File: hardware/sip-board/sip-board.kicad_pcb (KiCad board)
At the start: 8 copper layers, 17 x 50 mm, 110 parts, among them IC1 MT25QL512ABB1EW9-0SIT, IC2 XC7S15-1CPGA196C, IC3 LTC3569EUDC#TRPBF, J1 Conn_02x03_Odd_Even, J2 Conn_01x10_Pin, J3 Conn_01x10_Pin, J4 Conn_01x10_Pin, J5 Conn_01x10_Pin, Q1 MBT3904DW1, Q2 MBT3904DW1, Q5 BS170F

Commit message: WE REDOIN PCB
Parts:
- C10, C13, C15, C31, C32, C34, C36: footprint Capacitor_SMD:C_0201_0603Metric -> Capacitor_SMD:C_0402_1005Metric
- C11, C38: footprint Capacitor_SMD:C_0402_1005Metric -> Capacitor_SMD:C_0603_1608Metric; moved to B.Cu
- C2, C3, C39, C4, C5, C6, L1, L2, L3, R10, R11, R12, R13, R14, R15, R16, R17, R18, R19, R20, R25, R28, R30, R32, R4, R5, R6, R7, R8, R9, U10, U11, U12, U13, U4, U5, U6, U7, U8, U9: moved to F.Cu
- C28, C29, C30: footprint Capacitor_SMD:C_0402_1005Metric -> Capacitor_SMD:C_0603_1608Metric
- C33, C35: footprint Capacitor_SMD:C_0201_0603Metric -> Capacitor_SMD:C_0402_1005Metric; moved to F.Cu
- C37: footprint Capacitor_SMD:C_0201_0603Metric -> Capacitor_SMD:C_0603_1608Metric
- C8: footprint Capacitor_SMD:C_0201_0603Metric -> Capacitor_SMD:C_0603_1608Metric; moved to F.Cu
- moved R5 98.0 mm to (19.9, 57.5), turned to 0 degrees
- moved R7 97.2 mm to (19.9, 61.0), turned to 0 degrees
- moved R8 96.1 mm to (19.9, 62.8), turned to 0 degrees
- moved R9 95.2 mm to (19.9, 64.5), turned to 0 degrees
- moved C37 90.9 mm to (19.9, 54.0), turned to 0 degrees
- moved CFG1 90.6 mm to (25.1, 59.2), turned to 0 degrees
- moved U13 89.7 mm to (43.3, 40.2)
- moved U7 86.6 mm to (39.4, 36.5), turned to 0 degrees
- moved U12 85.8 mm to (43.3, 36.5)
- moved R20 85.3 mm to (40.9, 49.9), turned to 0 degrees
- moved J1 85.0 mm to (24.8, 67.7)
- moved U5 84.7 mm to (39.4, 29.2), turned to 0 degrees
- moved U11 81.6 mm to (43.3, 32.8)
- moved R19 81.5 mm to (40.9, 48.2), turned to 0 degrees
- moved R14 80.7 mm to (38.5, 48.2), turned to 0 degrees
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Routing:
- net +5V: track 141.0 -> 0.00 mm, vias 11 -> 0
- net GND: track 87.8 -> 0.00 mm, vias 97 -> 0
- net +3V3: track 61.4 -> 0.00 mm, vias 35 -> 0
- net SPI_DQ0: track 25.3 -> 0.00 mm, vias 2 -> 0
- net M0_CONFIG: track 24.9 -> 0.00 mm, vias 2 -> 0
- net M1_CONFIG: track 23.2 -> 0.00 mm, vias 4 -> 0
- net SPI_DQ3: track 23.2 -> 0.00 mm, vias 2 -> 0
- net SPI_DQ2: track 23.0 -> 0.00 mm, vias 2 -> 0
- net SPI_SCK_CCLK: track 22.7 -> 0.00 mm, vias 2 -> 0
- net SPI_DQ1: track 21.9 -> 0.00 mm, vias 2 -> 0
- net M2_CONFIG: track 21.8 -> 0.00 mm, vias 2 -> 0
- net +1V8: track 21.6 -> 0.00 mm, vias 6 -> 0
- net SPI_CS: track 21.2 -> 0.00 mm, vias 2 -> 0
- net +1V0: track 15.6 -> 0.00 mm, vias 12 -> 0
- net PROGRAM_B: track 15.1 -> 0.00 mm, vias 2 -> 0
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- removed copper zone on In3.Cu, net +1V0
- removed copper zone on In3.Cu, net +1V8
- removed copper zone on In4.Cu, net +3V3
- removed copper zone on In1.Cu, net GND
- removed copper zone on In6.Cu, net GND
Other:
- board text added: "3V3 1V8 1V0 GND"
- board text removed: "1V0"
- board text removed: "1V8"
- board text removed: "DQ0 SCK DQ3"
- board text removed: "DQ2 DQ1 __ CS"
- board text removed: "GND"
- board text removed: "INIT"
- board text removed: "JTAG"
- board text removed: "M2 M1 M0"
- board text removed: "M[2:0]=001 QSPI M[2:0]=101 JTAG"
- board text removed: "RESET"

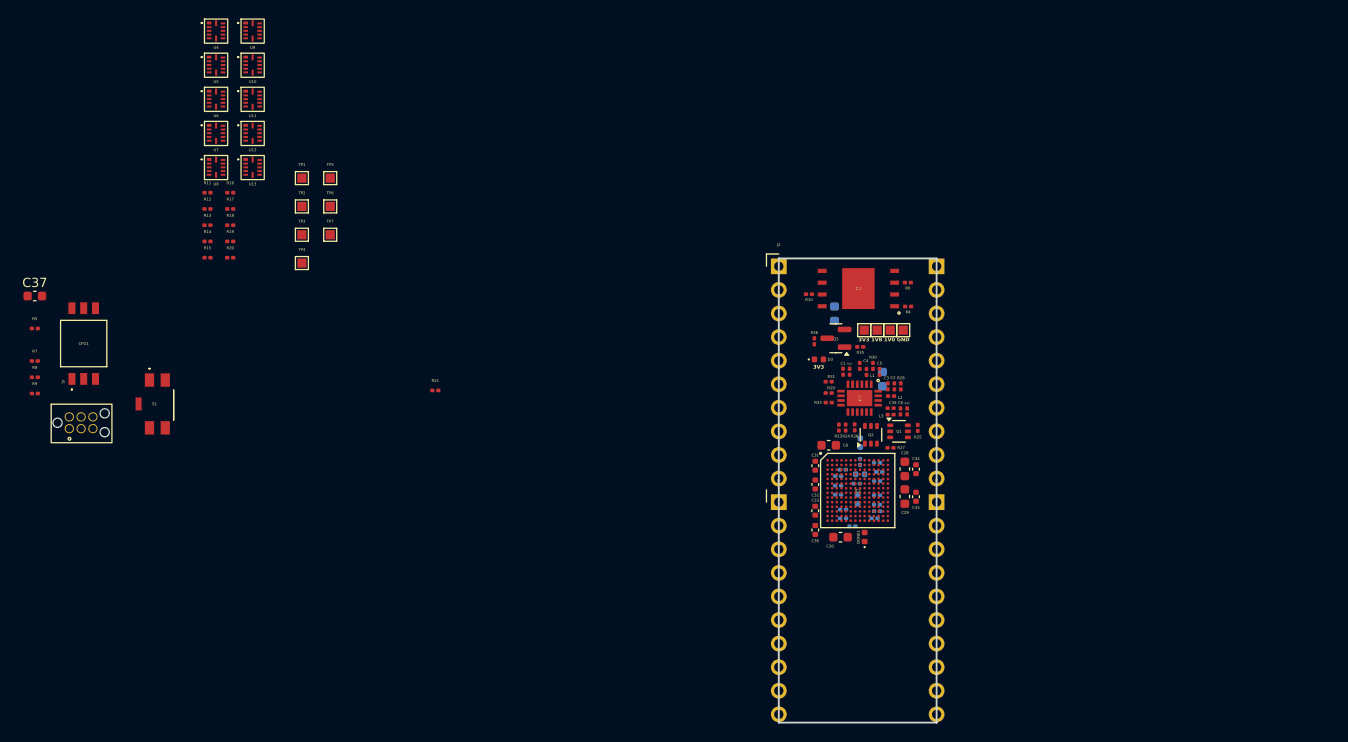
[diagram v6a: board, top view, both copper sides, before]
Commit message: redo layout of sip (again), changed switching reg to be on surface, need to route, need to add 2 more layers for 5V plane
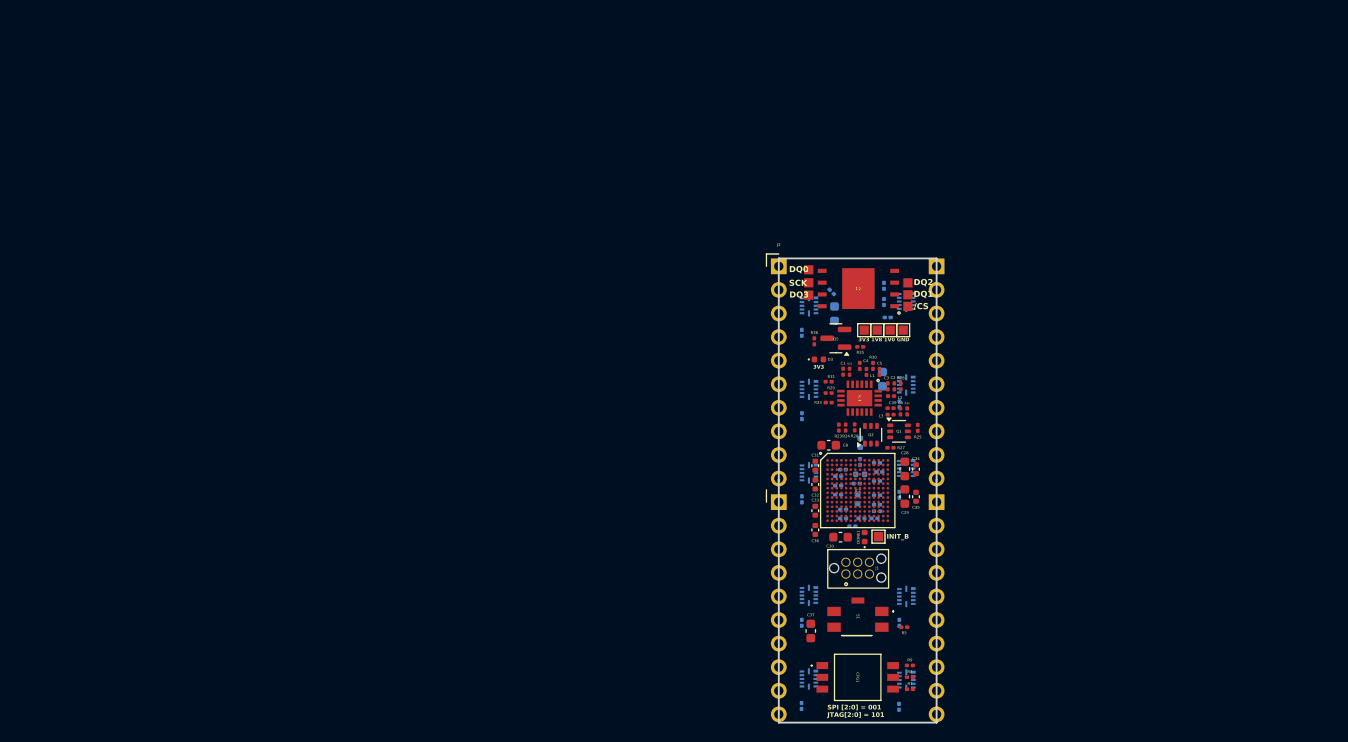
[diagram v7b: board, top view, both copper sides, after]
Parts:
- removed R18, R19, R20: 10k, Resistor_SMD:R_0201_0603Metric
- removed U4: ~, hardware:NXB0104GU12X
- added LVL3: ~, hardware:NXB0104GU12X, B.Cu at (103.2, 73.1)
- added R1: 100k, Resistor_SMD:R_0201_0603Metric, B.Cu at (102.5, 67.0)
- added R2: 100k, Resistor_SMD:R_0201_0603Metric, B.Cu at (102.5, 76.0)
- added R3: 100k, Resistor_SMD:R_0201_0603Metric, B.Cu at (102.5, 89.2)
- LVL1: renamed from U8; moved to B.Cu
- LVL10: renamed from U9; moved to B.Cu
- LVL2: renamed from U6; moved to B.Cu
- LVL4: renamed from U5; moved to B.Cu
- LVL5: renamed from U7; moved to B.Cu
- LVL6: renamed from U13; moved to B.Cu
- LVL7: renamed from U12; moved to B.Cu
- LVL8: renamed from U11; moved to B.Cu
- LVL9: renamed from U10; moved to B.Cu
- R10, R21, R4, R6: moved to B.Cu
- R11, R12, R13, R14, R15, R16, R17: value 10k -> 100k; moved to B.Cu
- moved R7 100.7 mm to (114.1, 96.4)
- moved R8 99.7 mm to (114.1, 95.1)
- moved R5 99.0 mm to (113.5, 89.7), turned to 180 degrees
- moved R9 98.7 mm to (114.1, 93.8)
- moved C37 91.0 mm to (103.4, 90.1), turned to -90 degrees
- moved CFG1 90.8 mm to (108.5, 95.1), turned to -90 degrees
- moved R17 89.8 mm to (112.9, 98.3), turned to 90 degrees
- moved LVL6 89.5 mm to (113.7, 95.4), turned to 180 degrees
- moved LVL5 86.8 mm to (103.2, 95.3), turned to 180 degrees
- moved LVL7 86.3 mm to (113.7, 86.4), turned to 180 degrees
- moved LVL4 85.7 mm to (103.2, 86.3), turned to 180 degrees
- moved R16 85.7 mm to (113.0, 89.2), turned to 90 degrees
- moved J1 85.1 mm to (108.5, 83.4)
- moved R11 84.6 mm to (102.5, 98.2), turned to 90 degrees
- moved LVL8 80.9 mm to (113.7, 72.6), turned to 180 degrees
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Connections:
- LVL10 pad 1: +3V3 -> +5V
- LVL10 pad 10: A8_5V -> A9_FPGA
- LVL10 pad 11: A7_5V -> A10_FPGA
- LVL10 pad 12: +5V -> +3V3
- LVL10 pad 2: A7_FPGA -> A10_5V
- LVL10 pad 3: A8_FPGA -> A9_5V
- LVL10 pad 4: A9_FPGA -> A8_5V
- LVL10 pad 5: A10_FPGA -> A7_5V
- LVL10 pad 7: Net-(U9-OE) -> Net-(LVL10-OE)
- LVL10 pad 8: A10_5V -> A7_FPGA
- LVL10 pad 9: A9_5V -> A8_FPGA
- LVL2 pad 7: Net-(U6-OE) -> Net-(LVL2-OE)
- LVL4 pad 7: Net-(U5-OE) -> Net-(LVL4-OE)
- LVL5 pad 7: Net-(U7-OE) -> Net-(LVL5-OE)
- LVL6 pad 1: +3V3 -> +5V
- LVL6 pad 10: WR_5V -> BUSAK_FPGA
- LVL6 pad 11: RD_5V -> WAIT_FPGA
- LVL6 pad 12: +5V -> +3V3
- LVL6 pad 2: RD_FPGA -> WAIT_5V
- LVL6 pad 3: WR_FPGA -> BUSAK_5V
- LVL6 pad 4: BUSAK_FPGA -> WR_5V
- LVL6 pad 5: WAIT_FPGA -> RD_5V
- LVL6 pad 7: Net-(U13-OE) -> Net-(LVL6-OE)
- LVL6 pad 8: WAIT_5V -> RD_FPGA
- LVL6 pad 9: BUSAK_5V -> WR_FPGA
- LVL7 pad 1: +3V3 -> +5V
- LVL7 pad 10: RESET_5V -> M1_FPGA
- LVL7 pad 11: BUSRQ_5V -> RFSH_FPGA
- LVL7 pad 12: +5V -> +3V3
- LVL7 pad 2: BUSRQ_FPGA -> RFSH_5V
- LVL7 pad 3: RESET_FPGA -> M1_5V
- LVL7 pad 4: M1_FPGA -> RESET_5V
- LVL7 pad 5: RFSH_FPGA -> BUSRQ_5V
- LVL7 pad 7: Net-(U12-OE) -> Net-(LVL7-OE)
- LVL7 pad 8: RFSH_5V -> BUSRQ_FPGA
- LVL7 pad 9: M1_5V -> RESET_FPGA
- LVL8 pad 1: +3V3 -> +5V
- LVL8 pad 10: A1_5V -> A2_FPGA
- LVL8 pad 11: A0_5V -> unconnected-(LVL8-B1-Pad11)
- LVL8 pad 12: +5V -> +3V3
- LVL8 pad 2: A0_FPGA -> unconnected-(LVL8-A1-Pad2)
- LVL8 pad 3: A1_FPGA -> A2_5V
- LVL8 pad 4: A2_FPGA -> A1_5V
- LVL8 pad 5: unconnected-(U11-A4-Pad5) -> A0_5V
- LVL8 pad 7: Net-(U11-OE) -> Net-(LVL8-OE)
- LVL8 pad 8: unconnected-(U11-B4-Pad8) -> A0_FPGA
- LVL8 pad 9: A2_5V -> A1_FPGA
- LVL9 pad 1: +3V3 -> +5V
- LVL9 pad 10: A4_5V -> A5_FPGA
- LVL9 pad 11: A3_5V -> A6_FPGA
- LVL9 pad 12: +5V -> +3V3
- LVL9 pad 2: A3_FPGA -> A6_5V
- LVL9 pad 3: A4_FPGA -> A5_5V
- LVL9 pad 4: A5_FPGA -> A4_5V
- LVL9 pad 5: A6_FPGA -> A3_5V
- LVL9 pad 7: Net-(U10-OE) -> Net-(LVL9-OE)
- LVL9 pad 8: A6_5V -> A3_FPGA
- LVL9 pad 9: A5_5V -> A4_FPGA
- R11 pad 2: Net-(U4-OE) -> Net-(LVL5-OE)
- R12 pad 1: +3V3 -> +5V
- R12 pad 2: Net-(U5-OE) -> Net-(LVL10-OE)
- R13 pad 1: +3V3 -> +5V
- R13 pad 2: Net-(U6-OE) -> Net-(LVL9-OE)
- R14 pad 1: +3V3 -> +5V
- R14 pad 2: Net-(U7-OE) -> Net-(LVL8-OE)
- R16 pad 1: +3V3 -> +5V
- R16 pad 2: Net-(U9-OE) -> Net-(LVL7-OE)
- R17 pad 1: +3V3 -> +5V
- R17 pad 2: Net-(U10-OE) -> Net-(LVL6-OE)
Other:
- board text added: "/CS"
- board text added: "DQ0"
- board text added: "DQ1"
- board text added: "DQ2"
- board text added: "DQ3"
- board text added: "INIT_B"
- board text added: "SCK"
- board text added: "SPI [2:0] = 001 JTAG[2:0] = 101"

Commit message: work on layout (im sad)
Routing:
- net +3V3: track 0.00 -> 41.5 mm, vias 0 -> 25
- net GND: track 0.00 -> 38.7 mm, vias 0 -> 104
- net +1V8: track 0.00 -> 28.6 mm, vias 0 -> 5
- net SPI_DQ0: track 0.00 -> 27.5 mm, vias 0 -> 2
- net SPI_DQ3: track 0.00 -> 25.2 mm, vias 0 -> 2
- net M1_CONFIG: track 0.00 -> 25.0 mm, vias 0 -> 2
- net SPI_DQ2: track 0.00 -> 23.9 mm, vias 0 -> 2
- net SPI_SCK_CCLK: track 0.00 -> 23.7 mm, vias 0 -> 2
- net M2_CONFIG: track 0.00 -> 23.7 mm, vias 0 -> 2
- net M0_CONFIG: track 0.00 -> 23.4 mm, vias 0 -> 2
- net SPI_DQ1: track 0.00 -> 22.8 mm, vias 0 -> 2
- net SPI_CS: track 0.00 -> 22.2 mm, vias 0 -> 2
- net /Voltage Regulators - 3V3, 1V8, 1V0/FB3: track 0.00 -> 21.9 mm, vias 0 -> 2
- net +1V0: track 0.00 -> 18.5 mm, vias 0 -> 15
- net PROGRAM_B: track 0.00 -> 16.3 mm, vias 0 -> 2
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- added copper zone on In3.Cu, net +1V0
- added copper zone on In4.Cu, net +3V3
- added copper zone on In7.Cu, net +5V
- added copper zone on In1.Cu, net GND
- added copper zone on In6.Cu, net GND
- added copper zone on In8.Cu, net GND
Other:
- copper layers 8 -> 10
- board text added: "2x GND plane - L2/7 3v3 plane - L5 5v plane - L8"
